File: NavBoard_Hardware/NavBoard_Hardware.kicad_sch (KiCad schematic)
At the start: 0 parts

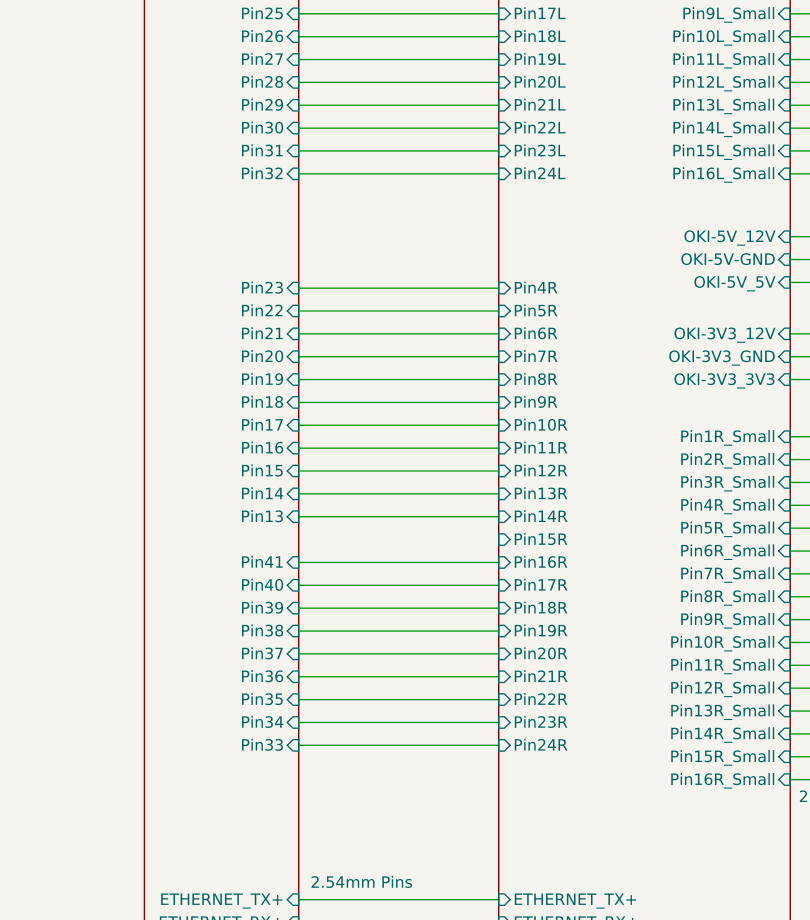
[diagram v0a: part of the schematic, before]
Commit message: Placed OKI SMD components, aligned ethernet pins
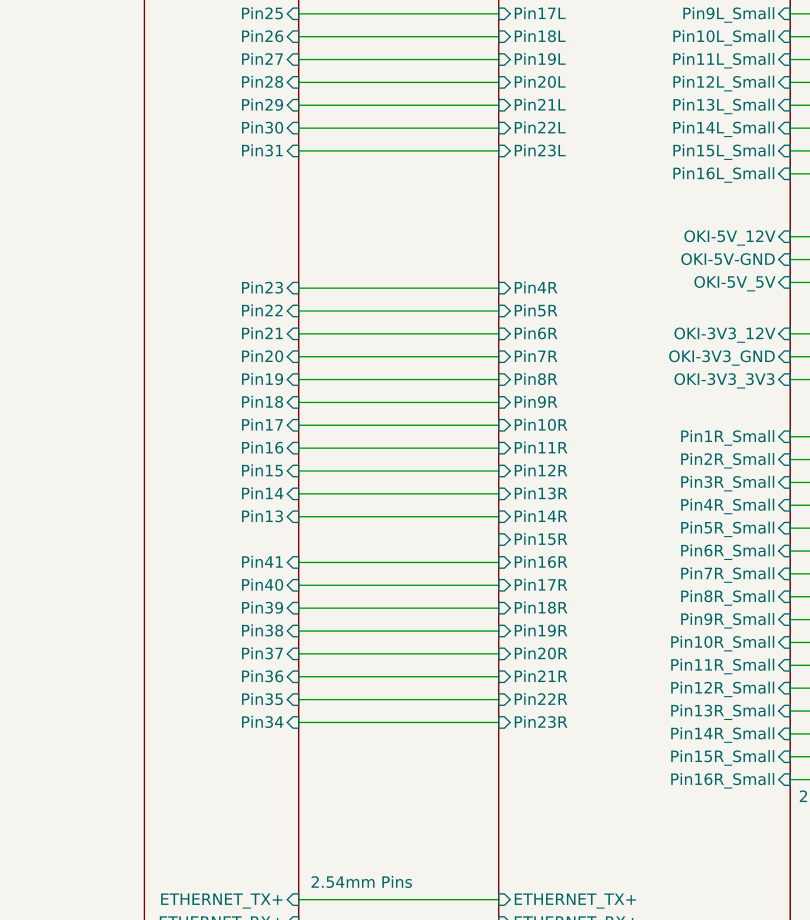
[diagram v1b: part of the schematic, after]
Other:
- sheet Main Board ports: added none; removed Pin24L, Pin24R
- sheet Teensy & Shield ports: added none; removed Pin32, Pin33
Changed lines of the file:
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@@
-    (stroke (width 0) (type default) (color 0 0 0 0))
-  )
-  (wire (pts (xy 95.885 86.995) (xy 118.11 86.995))
     (stroke (width 0) (type default) (color 0 0 0 0))
   )
@@
   )
   (wire (pts (xy 150.495 154.305) (xy 172.72 154.305))
-    (stroke (width 0) (type default) (color 0 0 0 0))
-  )
-  (wire (pts (xy 95.885 150.495) (xy 118.11 150.495))
     (stroke (width 0) (type default) (color 0 0 0 0))
   )
@@
       (effects (font (size 1.27 1.27)) (justify left))
     )
-    (pin "Pin24R" input (at 118.11 150.495 180)
-      (effects (font (size 1.27 1.27)) (justify left))
-    )
     (pin "Pin6R" input (at 118.11 104.775 180)
       (effects (font (size 1.27 1.27)) (justify left))
@@
     )
     (pin "Pin23L" input (at 118.11 84.455 180)
-      (effects (font (size 1.27 1.27)) (justify left))
-    )
-    (pin "Pin24L" input (at 118.11 86.995 180)
       (effects (font (size 1.27 1.27)) (justify left))
     )
@@
       (effects (font (size 1.27 1.27)) (justify right))
     )
-    (pin "Pin32" input (at 95.885 86.995 0)
-      (effects (font (size 1.27 1.27)) (justify right))
-    )
     (pin "Pin24" input (at 95.885 66.675 0)
       (effects (font (size 1.27 1.27)) (justify right))
@@
     )
     (pin "Pin34" input (at 95.885 147.955 0)
-      (effects (font (size 1.27 1.27)) (justify right))
-    )
-    (pin "Pin33" input (at 95.885 150.495 0)
       (effects (font (size 1.27 1.27)) (justify right))
     )
@@
       (reference "#PWR048") (unit 1) (value "GND") (footprint "")
     )
+    (path "/40b46045-12d0-4208-984c-573a30ffe5b1/ba418a55-1537-4060-8e95-cf03f98c2622"
+      (reference "#PWR0101") (unit 1) (value "GND") (footprint "")
+    )
+    (path "/40b46045-12d0-4208-984c-573a30ffe5b1/09373361-62c4-42de-b9b7-a729acaf39a7"
+      (reference "#PWR0102") (unit 1) (value "GND") (footprint "")
+    )
+    (path "/40b46045-12d0-4208-984c-573a30ffe5b1/c5dae13d-f1b7-4ad0-a449-0630c9adaab4"
+      (reference "#PWR0103") (unit 1) (value "GND") (footprint "")
+    )
+    (path "/40b46045-12d0-4208-984c-573a30ffe5b1/6af65c19-ff57-4693-8460-d9d099935dcf"
+      (reference "#PWR0104") (unit 1) (value "GND") (footprint "")
+    )
+    (path "/f643fe13-52b3-46d1-8243-a8bbe65cd5c3/2b7fcf09-e328-437d-92c8-775d9c373e6c"
+      (reference "#PWR0105") (unit 1) (value "GND") (footprint "")
+    )
+    (path "/f643fe13-52b3-46d1-8243-a8bbe65cd5c3/33d6b5f3-2e6e-4654-a364-155cb6e897fb"
+      (reference "#PWR0106") (unit 1) (value "GND") (footprint "")
+    )
+    (path "/1cf30331-e31a-4dae-8418-1a281b51585f/95aece0b-b52d-44f9-8cec-c562feeb9a81"
+      (reference "#PWR0107") (unit 1) (value "GND") (footprint "")
+    )
+    (path "/1cf30331-e31a-4dae-8418-1a281b51585f/e4842d6b-04ed-46ac-9bb8-00592c109531"
+      (reference "#PWR0108") (unit 1) (value "GND") (footprint "")
+    )
     (path "/1cf30331-e31a-4dae-8418-1a281b51585f/cfa695dc-e859-4ad7-a02d-ada1f7512f16/d997983e-985b-4240-8c4e-c57a43eedad7"
       (reference "C1") (unit 1) (value "0.1uF") (footprint "Capacitor_SMD:C_0603_1608Metric_Pad1.08x0.95mm_HandSolder")
@@
     )
     (path "/40b46045-12d0-4208-984c-573a30ffe5b1/357a43eb-a87c-4cdf-9487-a68be7ac6c3f/01cf29d6-65fd-424c-a1f9-49ef3759f2ec"
-      (reference "C5") (unit 1) (value "22uF 50V") (footprint "Capacitor_THT:CP_Radial_D6.3mm_P2.50mm")
+      (reference "C5") (unit 1) (value "22uF 50V") (footprint "Capacitor_SMD:C_1206_3216Metric_Pad1.33x1.80mm_HandSolder")
     )
     (path "/40b46045-12d0-4208-984c-573a30ffe5b1/357a43eb-a87c-4cdf-9487-a68be7ac6c3f/2e304444-7195-4027-b495-eddacb745316"
@@
     )
     (path "/40b46045-12d0-4208-984c-573a30ffe5b1/d0993be0-fd80-4bb6-942e-ed63dd778efa/8a8f956a-784e-4722-86b6-81529e5ab031"
-      (reference "C12") (unit 1) (value "22uF 50V") (footprint "Capacitor_THT:CP_Radial_D6.3mm_P2.50mm")
+      (reference "C12") (unit 1) (value "22uF 50V") (footprint "Capacitor_SMD:C_1206_3216Metric_Pad1.33x1.80mm_HandSolder")
     )
     (path "/40b46045-12d0-4208-984c-573a30ffe5b1/d0993be0-fd80-4bb6-942e-ed63dd778efa/adf6e372-11b0-4024-890b-fadc141fe3b6"

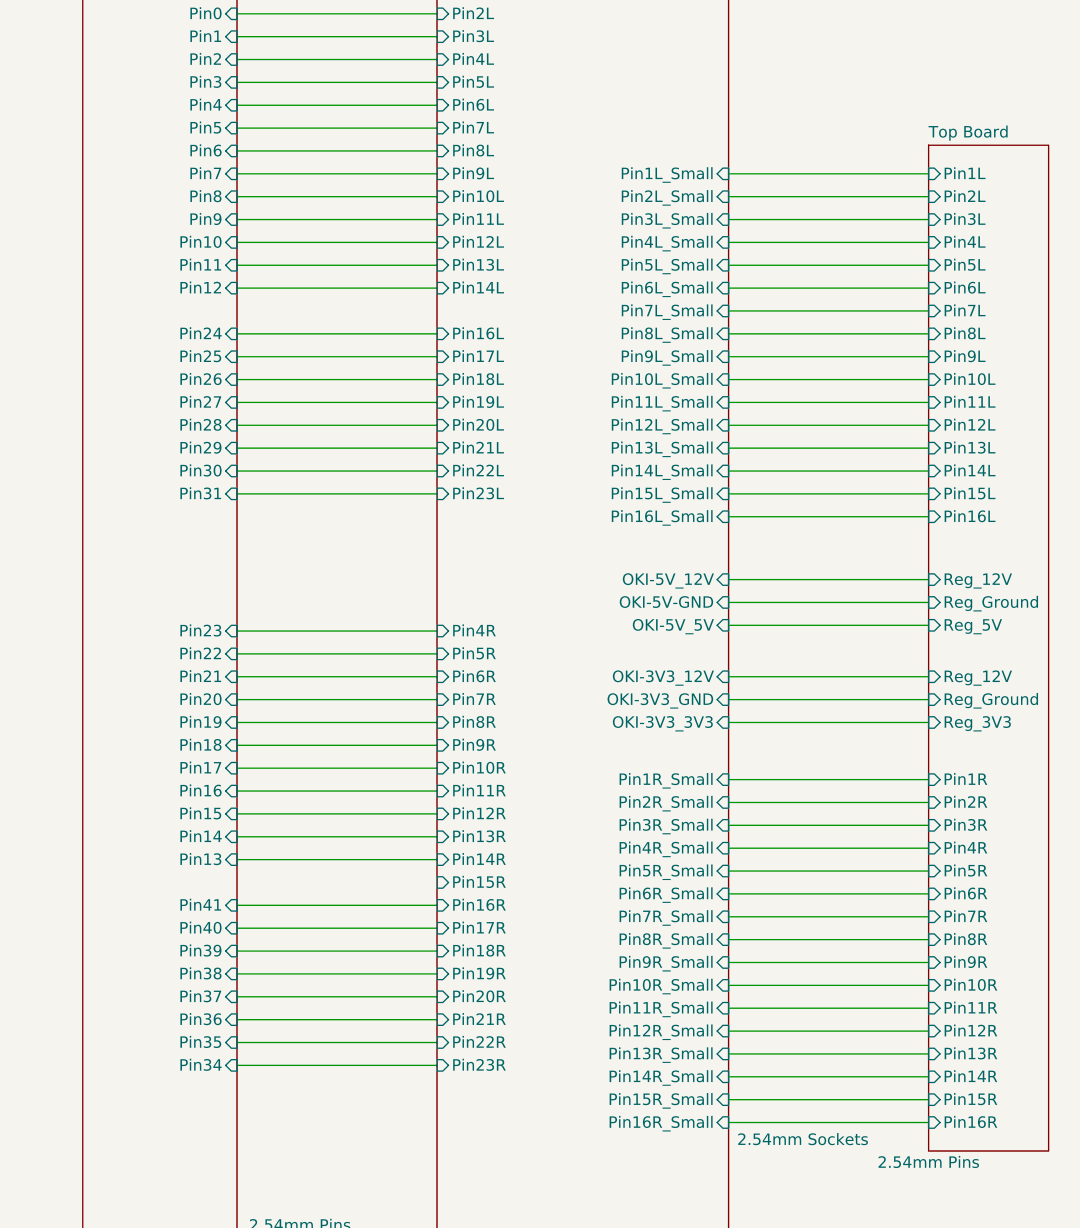
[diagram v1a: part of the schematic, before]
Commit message: Completed routing, added 3D models to IMUs
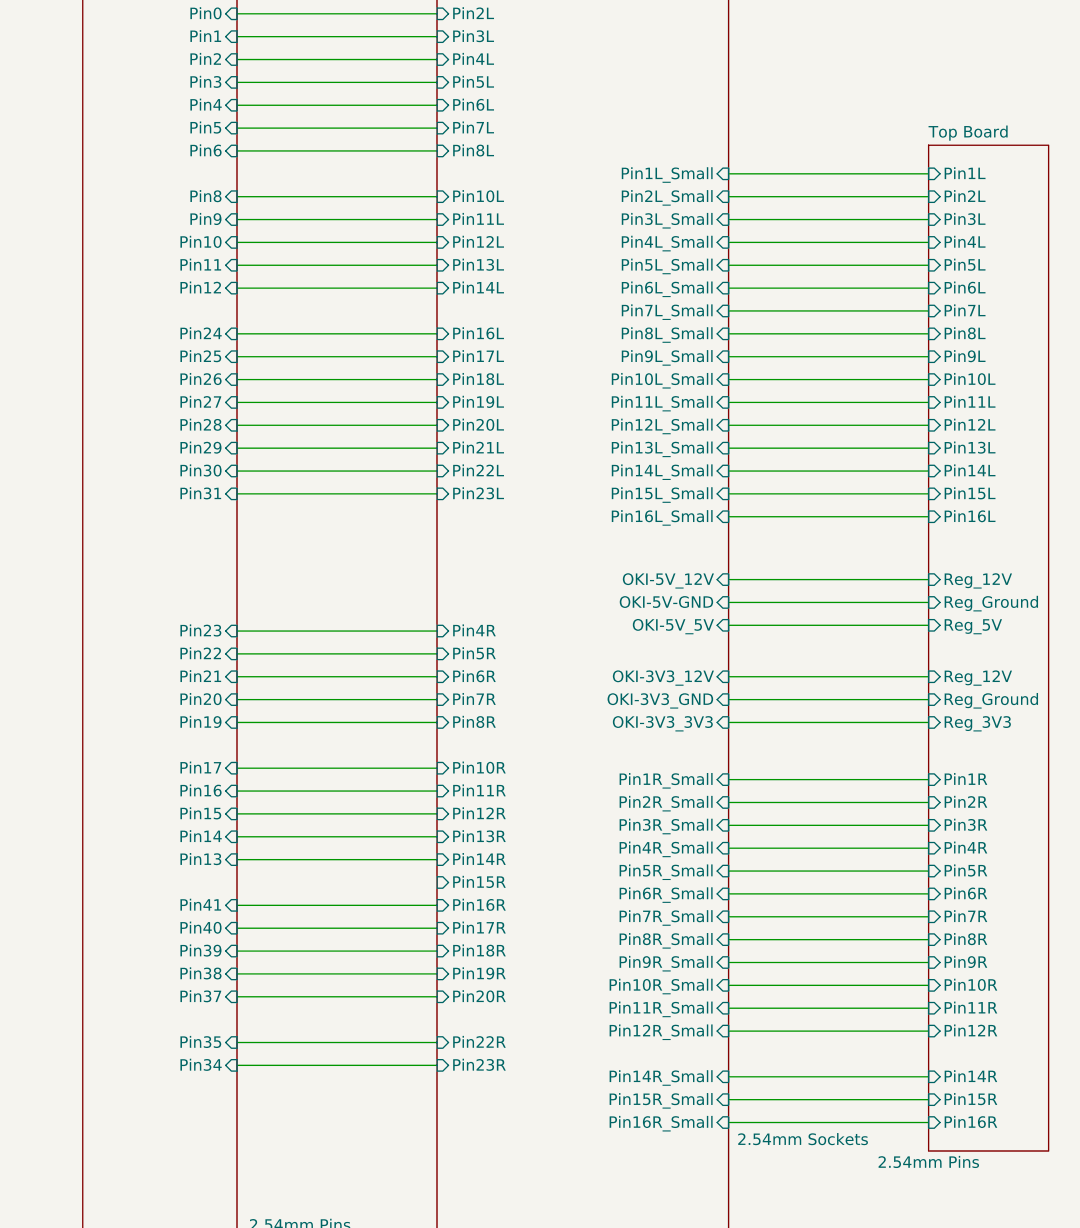
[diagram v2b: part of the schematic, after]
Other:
- sheet Main Board ports: added none; removed Pin13R_Small, Pin21R, Pin9L, Pin9R
- sheet Teensy & Shield ports: added none; removed Pin18, Pin36, Pin7
- sheet Top Board ports: added none; removed Pin13R
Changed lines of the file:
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@@
-    (stroke (width 0) (type default) (color 0 0 0 0))
-  )
-  (wire (pts (xy 150.495 146.685) (xy 172.72 146.685))
     (stroke (width 0) (type default) (color 0 0 0 0))
   )
@@
     (stroke (width 0) (type default) (color 0 0 0 0))
   )
-  (wire (pts (xy 95.885 112.395) (xy 118.11 112.395))
-    (stroke (width 0) (type default) (color 0 0 0 0))
-  )
   (wire (pts (xy 95.885 69.215) (xy 118.11 69.215))
     (stroke (width 0) (type default) (color 0 0 0 0))
@@
     (stroke (width 0) (type default) (color 0 0 0 0))
   )
-  (wire (pts (xy 95.885 48.895) (xy 118.11 48.895))
-    (stroke (width 0) (type default) (color 0 0 0 0))
-  )
   (wire (pts (xy 150.495 109.855) (xy 172.72 109.855))
     (stroke (width 0) (type default) (color 0 0 0 0))
@@
   )
   (wire (pts (xy 150.495 154.305) (xy 172.72 154.305))
-    (stroke (width 0) (type default) (color 0 0 0 0))
-  )
-  (wire (pts (xy 95.885 142.875) (xy 118.11 142.875))
     (stroke (width 0) (type default) (color 0 0 0 0))
   )
@@
       (effects (font (size 1.27 1.27)) (justify left))
     )
-    (pin "Pin13R" input (at 172.72 146.685 180)
-      (effects (font (size 1.27 1.27)) (justify left))
-    )
     (pin "Pin15R" input (at 172.72 151.765 180)
       (effects (font (size 1.27 1.27)) (justify left))
@@
       (effects (font (size 1.27 1.27)) (justify left))
     )
-    (pin "Pin9R" input (at 118.11 112.395 180)
-      (effects (font (size 1.27 1.27)) (justify left))
-    )
     (pin "Pin8R" input (at 118.11 109.855 180)
       (effects (font (size 1.27 1.27)) (justify left))
@@
       (effects (font (size 1.27 1.27)) (justify left))
     )
-    (pin "Pin9L" input (at 118.11 48.895 180)
-      (effects (font (size 1.27 1.27)) (justify left))
-    )
     (pin "Pin8L" input (at 118.11 46.355 180)
       (effects (font (size 1.27 1.27)) (justify left))
@@
       (effects (font (size 1.27 1.27)) (justify left))
     )
-    (pin "Pin21R" input (at 118.11 142.875 180)
-      (effects (font (size 1.27 1.27)) (justify left))
-    )
     (pin "Pin22R" input (at 118.11 145.415 180)
       (effects (font (size 1.27 1.27)) (justify left))
@@
     )
     (pin "Pin6R_Small" input (at 150.495 128.905 0)
-      (effects (font (size 1.27 1.27)) (justify right))
-    )
-    (pin "Pin13R_Small" input (at 150.495 146.685 0)
       (effects (font (size 1.27 1.27)) (justify right))
     )
@@
       (effects (font (size 1.27 1.27)) (justify right))
     )
-    (pin "Pin18" input (at 95.885 112.395 0)
-      (effects (font (size 1.27 1.27)) (justify right))
-    )
     (pin "Pin22" input (at 95.885 102.235 0)
       (effects (font (size 1.27 1.27)) (justify right))
@@
       (effects (font (size 1.27 1.27)) (justify right))
     )
-    (pin "Pin7" input (at 95.885 48.895 0)
-      (effects (font (size 1.27 1.27)) (justify right))
-    )
     (pin "Pin5" input (at 95.885 43.815 0)
       (effects (font (size 1.27 1.27)) (justify right))
@@
     )
     (pin "Pin35" input (at 95.885 145.415 0)
-      (effects (font (size 1.27 1.27)) (justify right))
-    )
-    (pin "Pin36" input (at 95.885 142.875 0)
       (effects (font (size 1.27 1.27)) (justify right))
     )
@@
       (reference "#PWR040") (unit 1) (value "GND") (footprint "")
     )
-    (path "/1cf30331-e31a-4dae-8418-1a281b51585f/befc0306-57fa-4e1d-8486-5522b5021eb8"
-      (reference "#PWR041") (unit 1) (value "+3V3") (footprint "")
-    )
     (path "/1cf30331-e31a-4dae-8418-1a281b51585f/b21c0162-992b-4778-b165-321527686ed9"
       (reference "#PWR042") (unit 1) (value "GND") (footprint "")
@@
       (reference "#PWR048") (unit 1) (value "GND") (footprint "")
     )
+    (path "/f643fe13-52b3-46d1-8243-a8bbe65cd5c3/92a66736-515a-4ced-90ec-9b82902bc7aa"
+      (reference "#PWR049") (unit 1) (value "GND") (footprint "")
+    )
+    (path "/f643fe13-52b3-46d1-8243-a8bbe65cd5c3/cc77ec0e-853d-456e-834a-350d5562cac7"
+      (reference "#PWR050") (unit 1) (value "GND") (footprint "")
+    )
     (path "/40b46045-12d0-4208-984c-573a30ffe5b1/ba418a55-1537-4060-8e95-cf03f98c2622"
       (reference "#PWR0101") (unit 1) (value "GND") (footprint "")
@@
       (reference "#PWR0108") (unit 1) (value "GND") (footprint "")
     )
+    (path "/40b46045-12d0-4208-984c-573a30ffe5b1/be4c174b-9a70-42f9-83d1-2b6addebd0bf"
+      (reference "#PWR0109") (unit 1) (value "GND") (footprint "")
+    )
+    (path "/40b46045-12d0-4208-984c-573a30ffe5b1/371a65af-0c89-4968-ad16-067f29fab45a"
+      (reference "#PWR0110") (unit 1) (value "GND") (footprint "")
+    )
+    (path "/40b46045-12d0-4208-984c-573a30ffe5b1/fd46c51e-2998-4ef5-ab6f-c7b29734242f"
+      (reference "#PWR0111") (unit 1) (value "GND") (footprint "")
+    )
+    (path "/40b46045-12d0-4208-984c-573a30ffe5b1/908c5140-37ea-497e-9179-d12e5b0b8ddf"
+      (reference "#PWR0112") (unit 1) (value "GND") (footprint "")
+    )
+    (path "/f643fe13-52b3-46d1-8243-a8bbe65cd5c3/f1a9a46e-b373-42b1-97a3-4c357122255c"
+      (reference "#PWR0113") (unit 1) (value "GND") (footprint "")
+    )
+    (path "/f643fe13-52b3-46d1-8243-a8bbe65cd5c3/9f2c9686-bda0-4daa-a563-78a89abb6870"
+      (reference "#PWR0114") (unit 1) (value "GND") (footprint "")
+    )
+    (path "/1cf30331-e31a-4dae-8418-1a281b51585f/56a938ea-1593-4fd2-8ea5-ab347d02104e"
+      (reference "#PWR0115") (unit 1) (value "GND") (footprint "")
+    )
+    (path "/1cf30331-e31a-4dae-8418-1a281b51585f/e1142c7a-f6b4-4bcd-9600-761da2d08ca7"
+      (reference "#PWR0116") (unit 1) (value "GND") (footprint "")
+    )
     (path "/1cf30331-e31a-4dae-8418-1a281b51585f/cfa695dc-e859-4ad7-a02d-ada1f7512f16/d997983e-985b-4240-8c4e-c57a43eedad7"
       (reference "C1") (unit 1) (value "0.1uF") (footprint "Capacitor_SMD:C_0603_1608Metric_Pad1.08x0.95mm_HandSolder")
@@
       (reference "J3") (unit 1) (value "Ethernet Jack w/ Magnetics") (footprint "Connector_RJ:RJ45_Cetus_J1B1211CCD_Horizontal")
     )
-    (path "/f643fe13-52b3-46d1-8243-a8bbe65cd5c3/ca73e204-cb87-497e-a961-d6950d15ad5d"
+    (path "/f643fe13-52b3-46d1-8243-a8bbe65cd5c3/4ebf4e86-f3d0-4e6d-9936-dfabb1124e56"
       (reference "J4") (unit 1) (value "Teensy-2.54mm_Adapter") (footprint "Nav_Board:Teensy-2.54mm_Adapter")
     )
-    (path "/f643fe13-52b3-46d1-8243-a8bbe65cd5c3/b98faba9-1286-46c4-bf1b-05da7c0c1785"
+    (path "/f643fe13-52b3-46d1-8243-a8bbe65cd5c3/ae675f6f-064a-4f58-be5a-8b7725d93444"
       (reference "J4") (unit 2) (value "Teensy-2.54mm_Adapter") (footprint "Nav_Board:Teensy-2.54mm_Adapter")
+    )
+    (path "/f643fe13-52b3-46d1-8243-a8bbe65cd5c3/ed319102-3186-41cf-aa25-356966f96855"
+      (reference "J4") (unit 3) (value "Teensy-2.54mm_Adapter") (footprint "Nav_Board:Teensy-2.54mm_Adapter")
     )
     (path "/f643fe13-52b3-46d1-8243-a8bbe65cd5c3/44c5f4fd-8f37-434e-a7f1-2821029d5e51"
@@
       (reference "J9") (unit 1) (value "6 Pin Molex Micro-Fit") (footprint "Connector_Molex:Molex_Micro-Fit_3.0_43650-0600_1x06_P3.00mm_Horizontal")
     )
-    (path "/1cf30331-e31a-4dae-8418-1a281b51585f/fc5a0194-7f1f-41ed-a352-74d1778bc892"
-      (reference "JP1") (unit 1) (value "Solder Jumper") (footprint "Jumper:SolderJumper-2_P1.3mm_Open_RoundedPad1.0x1.5mm")
-    )
-    (path "/1cf30331-e31a-4dae-8418-1a281b51585f/7dda84c9-55d8-4b4c-9eba-7c65b23f909c"
-      (reference "JP2") (unit 1) (value "Solder Jumper") (footprint "Jumper:SolderJumper-2_P1.3mm_Open_RoundedPad1.0x1.5mm")
-    )
     (path "/1cf30331-e31a-4dae-8418-1a281b51585f/cfa695dc-e859-4ad7-a02d-ada1f7512f16/201fdf1e-2829-4fa2-96fb-a2a60a1b14d8"
       (reference "R1") (unit 1) (value "4.7k") (footprint "Resistor_SMD:R_0603_1608Metric_Pad0.98x0.95mm_HandSolder")
@@
     )
     (path "/1cf30331-e31a-4dae-8418-1a281b51585f/cfa695dc-e859-4ad7-a02d-ada1f7512f16/fadf7f4a-6125-4ad1-993e-1fb21ca0eeb8"
-      (reference "TP1") (unit 1) (value "TestPoint") (footprint "TestPoint:TestPoint_Pad_D2.0mm")
+      (reference "TP1") (unit 1) (value "TestPoint") (footprint "TestPoint:TestPoint_Pad_D1.5mm")
     )
     (path "/1cf30331-e31a-4dae-8418-1a281b51585f/cfa695dc-e859-4ad7-a02d-ada1f7512f16/91b985ca-4c09-4239-a304-0e08e3bbb010"
-      (reference "TP2") (unit 1) (value "TestPoint") (footprint "TestPoint:TestPoint_Pad_D2.0mm")
+      (reference "TP2") (unit 1) (value "TestPoint") (footprint "TestPoint:TestPoint_Pad_D1.5mm")
     )
     (path "/1cf30331-e31a-4dae-8418-1a281b51585f/86eac231-1167-4d7a-9297-0b8976912df5/f41a7e57-a3a1-40ed-a9c3-e457da089c6b"
-      (reference "TP3") (unit 1) (value "TestPoint") (footprint "TestPoint:TestPoint_Pad_D2.0mm")
+      (reference "TP3") (unit 1) (value "TestPoint") (footprint "TestPoint:TestPoint_Pad_D1.5mm")
     )
     (path "/1cf30331-e31a-4dae-8418-1a281b51585f/86eac231-1167-4d7a-9297-0b8976912df5/885ec225-9a08-444e-9280-4e97097e1285"
-      (reference "TP4") (unit 1) (value "TestPoint") (footprint "TestPoint:TestPoint_Pad_D2.0mm")
+      (reference "TP4") (unit 1) (value "TestPoint") (footprint "TestPoint:TestPoint_Pad_D1.5mm")
     )
     (path "/1cf30331-e31a-4dae-8418-1a281b51585f/cfa695dc-e859-4ad7-a02d-ada1f7512f16/6b570b0e-b046-4f1e-aa27-616110d3e310"

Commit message: Annotated schematic pages
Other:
- company: MRDT -> Thomas Francois, Missouri S&T Mars Rover Design Team
- title: NavBoard -> MRDT NavBoard
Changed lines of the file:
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@@
   (paper "A4")
   (title_block
-    (title "NavBoard")
-    (rev "1")
-    (company "MRDT")
+    (title "MRDT NavBoard")
+    (date "2022-10-08")
+    (rev "1, 2023")
+    (company "Thomas Francois, Missouri S&T Mars Rover Design Team")
+    (comment 1 "Teensy 4.1 Daughter Boards and Modules")
+    (comment 2 "and accelerometers")
+    (comment 3 "These boards are to be stacked together, and connects the Teensy to power, ethernet, ")
   )
   (wire (pts (xy 150.495 81.915) (xy 172.72 81.915))
